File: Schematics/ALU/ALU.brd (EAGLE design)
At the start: 309.4 x 168.8 mm, 65 parts

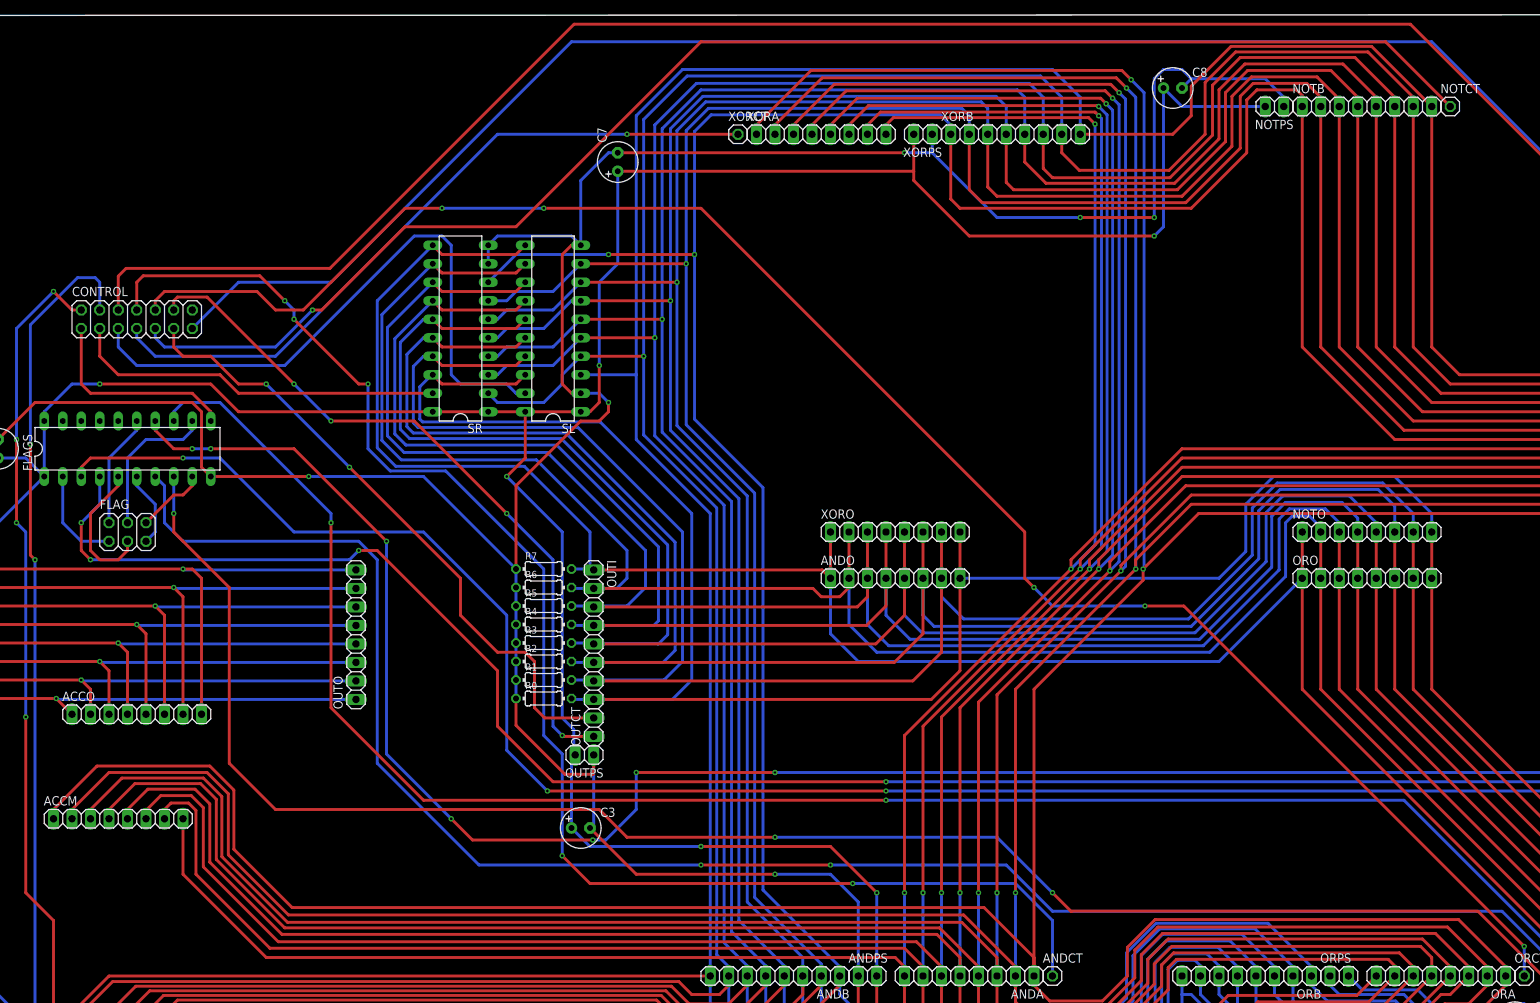
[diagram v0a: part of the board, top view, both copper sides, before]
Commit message: Fixed ACC mid pins now in correct order, Adder still have ACC and BUS switched.
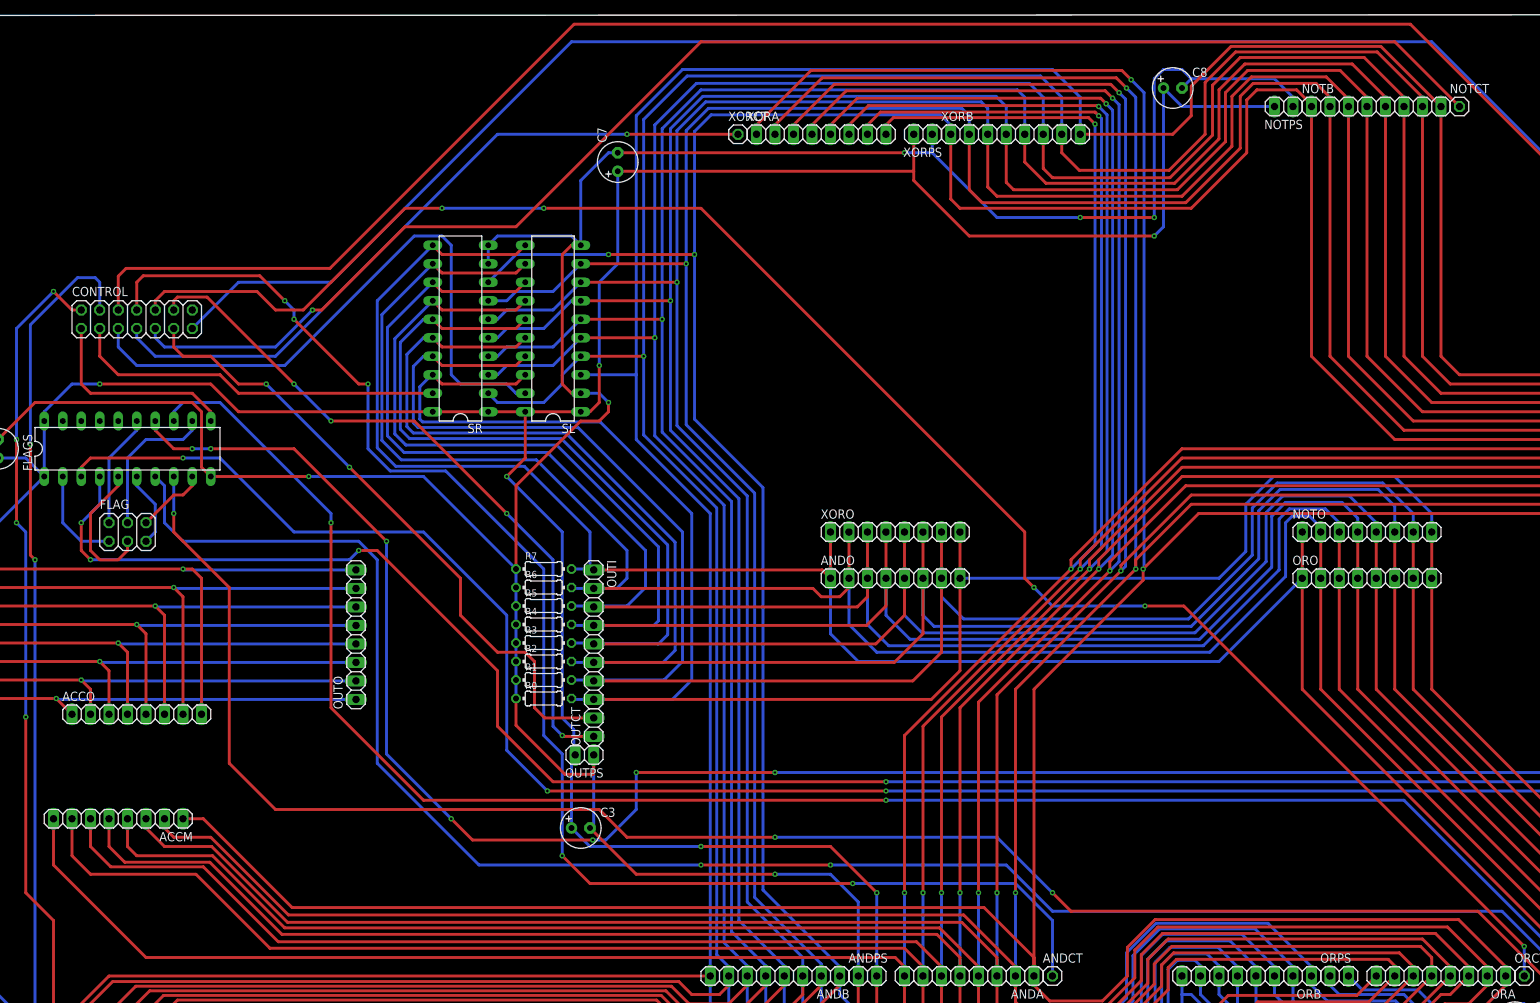
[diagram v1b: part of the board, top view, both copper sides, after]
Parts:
- moved NOTB 1.27 mm to (208.3, 156.2)
- moved NOTCT 1.27 mm to (219.7, 156.2)
- moved NOTPS 1.27 mm to (195.6, 156.2)
- turned ACCM to 180 degrees
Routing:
- net A7: track 529.1 -> 499.8 mm
- net A6: track 519.3 -> 496.4 mm
- net A5: track 510.8 -> 493.7 mm
- net A0: track 467.6 -> 484.7 mm
- net A4: track 499.5 -> 489.7 mm
- net A1: track 506.1 -> 514.1 mm
- net A3: track 527.9 -> 523.9 mm
- net A2: track 514.9 -> 516.7 mm
- net VCC: track 753.6 -> 754.8 mm
- net NOT-OE: track 200.6 -> 201.9 mm
- net GND: track 793.5 -> 794.7 mm
- net B5: track 649.1 -> 649.8 mm
- net B4: track 641.3 -> 642.0 mm
- net B1: track 630.0 -> 630.8 mm
- net B6: track 655.7 -> 656.5 mm
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
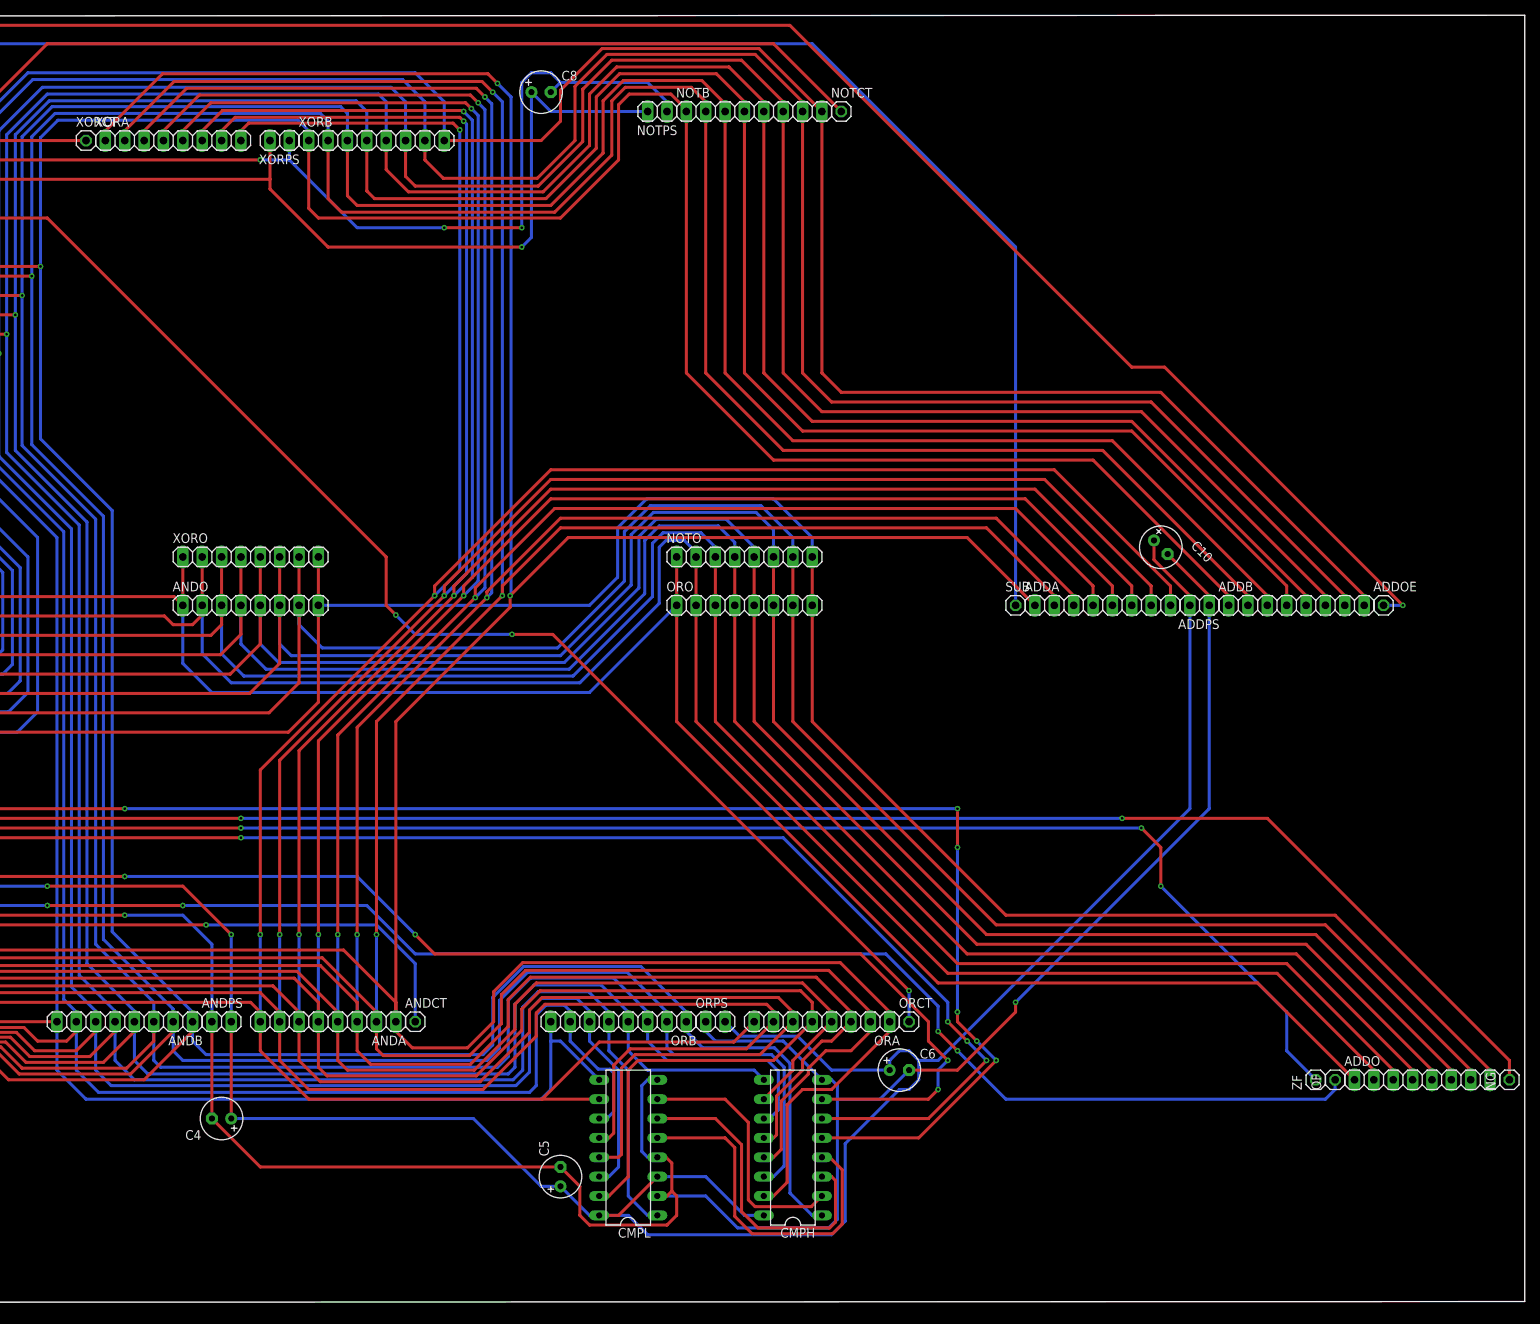
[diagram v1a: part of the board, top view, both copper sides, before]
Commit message: Fixed Adder inputs and added LEDs for ZF, OF and NF.
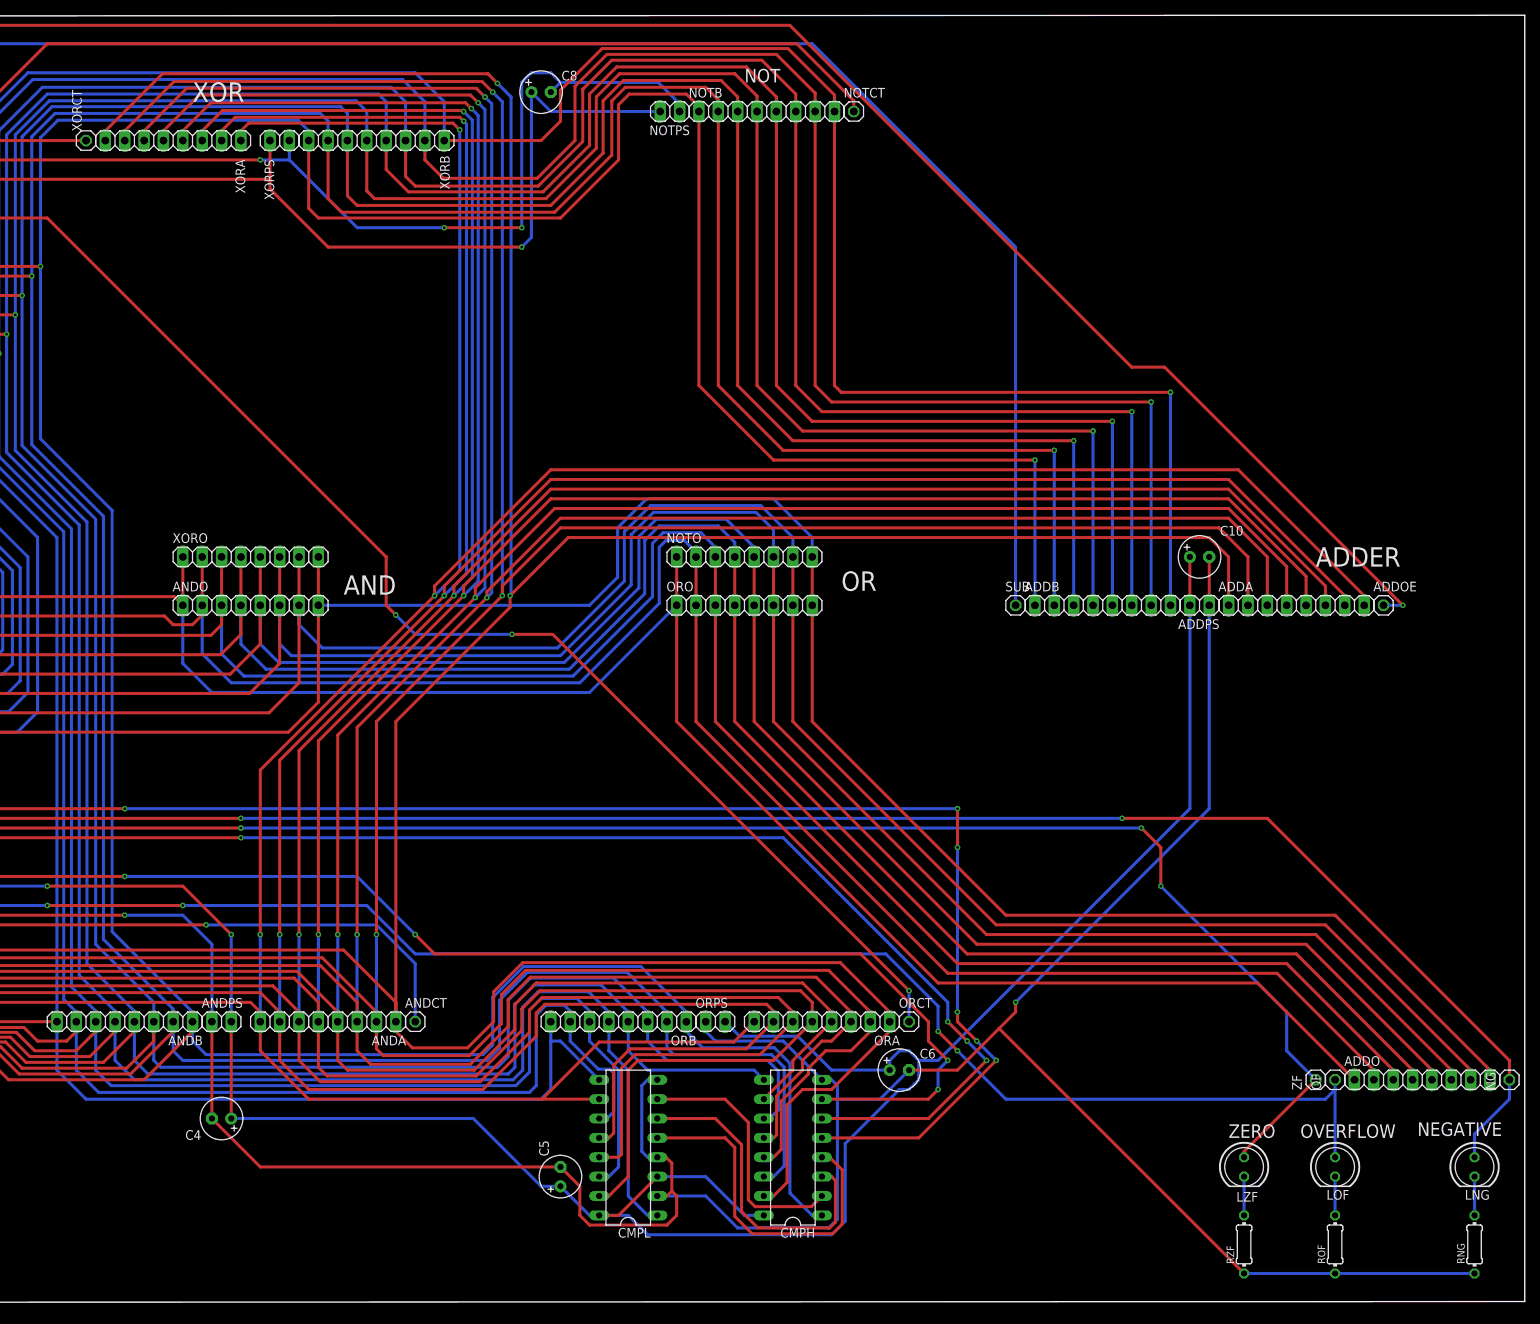
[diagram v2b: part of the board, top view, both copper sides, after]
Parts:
- added LNG, LOF, LZF: (no value), led:LED5MM
- added RNG, ROF, RZF: (no value), rcl:0204/7
- moved ADDA 25.4 mm to (279.4, 91.4)
- moved ADDB 25.4 mm to (254.0, 91.4)
- moved C10 5.24 mm to (266.7, 97.8), turned to 0 degrees
- moved NOTB 1.65 mm to (209.9, 156.2)
- moved NOTCT 1.65 mm to (221.4, 156.2)
- moved NOTPS 1.65 mm to (197.2, 156.2)
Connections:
- new net N$1: LOF.K, ROF.2
- new net N$2: LZF.K, RZF.2
- new net N$3: LNG.K, RNG.2
- net GND: now also RNG.1, ROF.1, RZF.1
- net NG: now also LNG.A
- net OF: now also LOF.A
- net ZF: now also LZF.A
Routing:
- net GND: track 794.7 -> 869.3 mm
- net A7: track 499.8 -> 529.0 mm
- net A6: track 496.4 -> 524.8 mm
- net A5: track 493.7 -> 522.1 mm
- net A4: track 489.7 -> 516.5 mm
- net A3: track 523.9 -> 550.0 mm
- net A2: track 516.7 -> 542.1 mm
- net A1: track 514.1 -> 538.7 mm
- net A0: track 484.7 -> 509.3 mm
- net ZF: track 302.7 -> 316.7 mm
- net B7: track 659.5 -> 645.7 mm, vias 2 -> 3
- net B6: track 656.5 -> 643.3 mm, vias 1 -> 2
- net B4: track 642.0 -> 630.0 mm, vias 1 -> 2
- net NG: track 322.4 -> 334.5 mm
- net B5: track 649.8 -> 637.8 mm, vias 1 -> 2
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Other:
- board text added: "ADDER"
- board text added: "AND"
- board text added: "NEGATIVE"
- board text added: "NOT"
- board text added: "OR"
- board text added: "OVERFLOW"
- board text added: "XOR"
- board text added: "ZERO"
